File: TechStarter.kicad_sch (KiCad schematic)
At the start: 3 parts, among them U1 STM32F446RETx, U2 TMC2209-LA, U3 TMC2209-LA

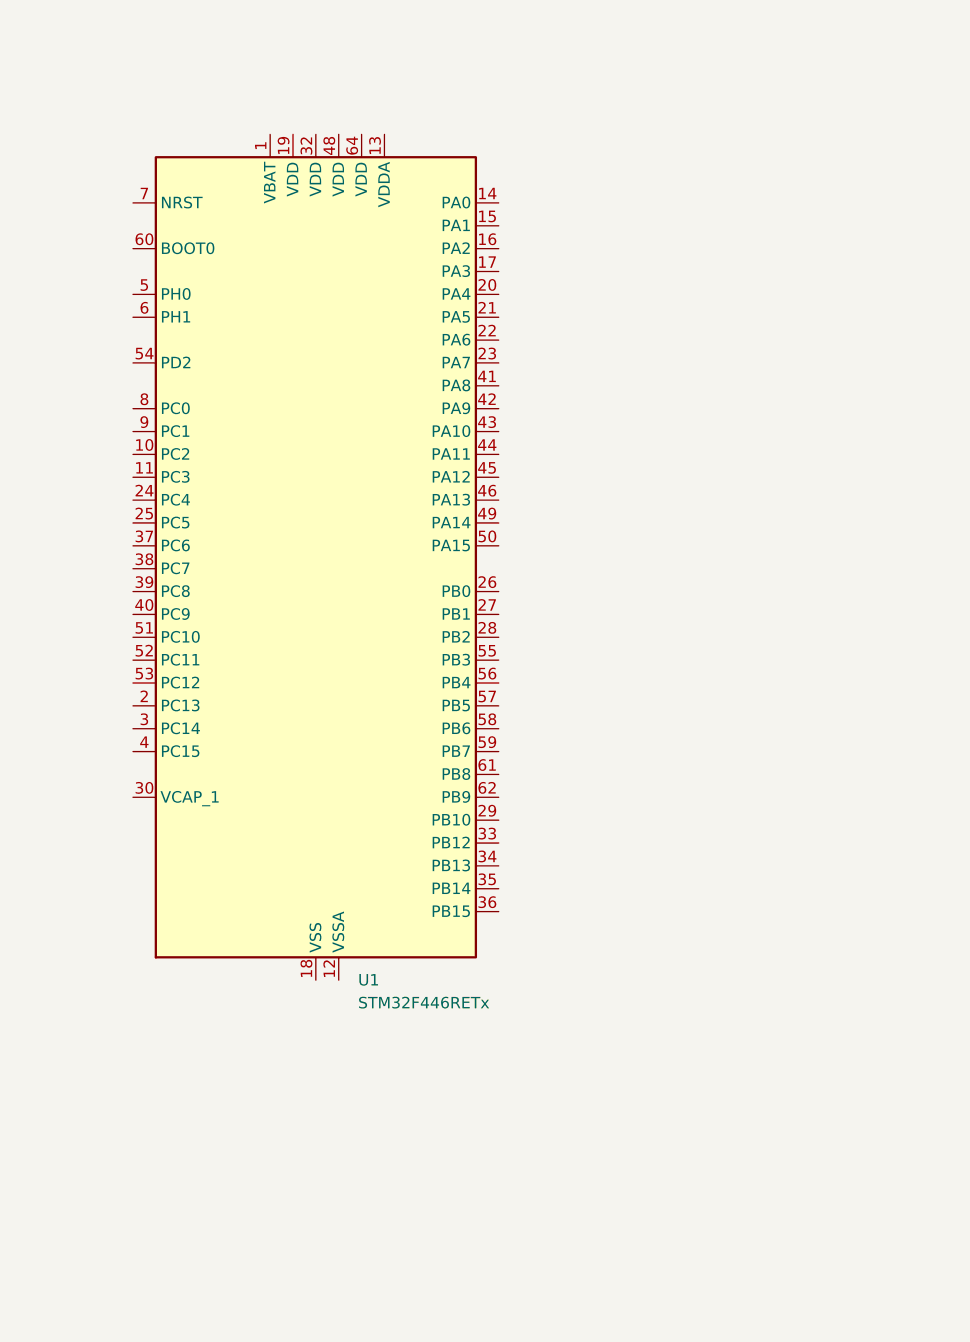
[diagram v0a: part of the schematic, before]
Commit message: added start of power brick
without values
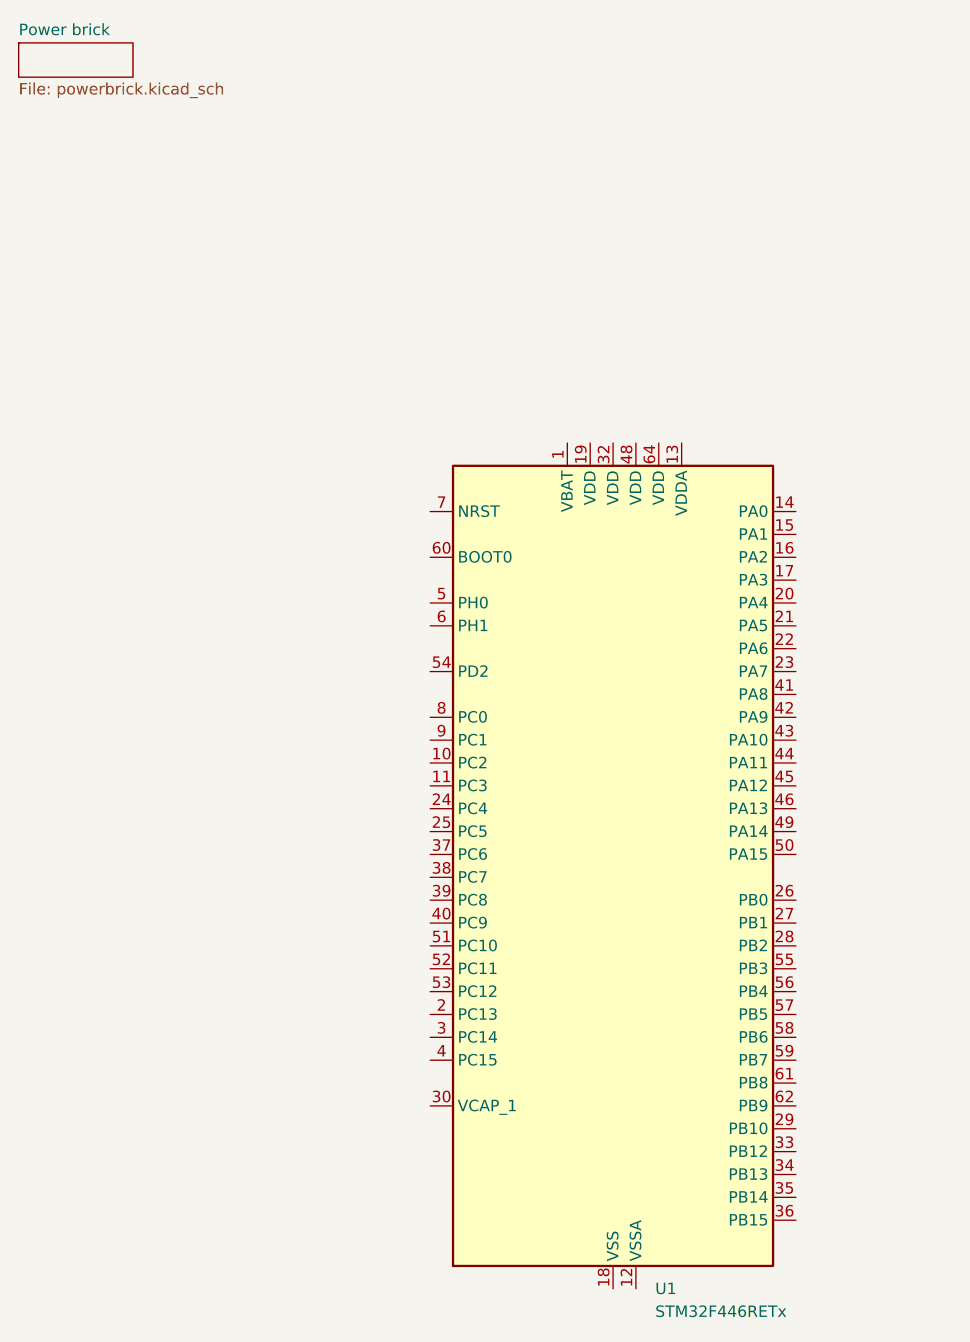
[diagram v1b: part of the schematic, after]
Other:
- added sheet Power brick (powerbrick.kicad_sch)
- moved on the sheet: U1
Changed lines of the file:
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@@
 	(symbol
 		(lib_id "MCU_ST_STM32F4:STM32F446RETx")
-		(at 54.61 80.01 0)
+		(at 87.63 114.3 0)
 		(unit 1)
 		(exclude_from_sim no)
@@
 		(fields_autoplaced yes)
 		(property "Reference" "U1"
-			(at 59.2933 125.73 0)
+			(at 92.3133 160.02 0)
 			(effects
 				(font
@@
 		)
 		(property "Value" "STM32F446RETx"
-			(at 59.2933 128.27 0)
+			(at 92.3133 162.56 0)
 			(effects
 				(font
@@
 		)
 		(property "Footprint" "Package_QFP:LQFP-64_10x10mm_P0.5mm"
-			(at 36.83 123.19 0)
+			(at 69.85 157.48 0)
 			(effects
 				(font
@@
 		)
 		(property "Datasheet" "https://www.st.com/resource/en/datasheet/stm32f446re.pdf"
-			(at 54.61 80.01 0)
+			(at 87.63 114.3 0)
 			(effects
 				(font
@@
 		)
 		(property "Description" "STMicroelectronics Arm Cortex-M4 MCU, 512KB flash, 128KB RAM, 180 MHz, 1.8-3.6V, 50 GPIO, LQFP64"
-			(at 54.61 80.01 0)
+			(at 87.63 114.3 0)
 			(effects
 				(font
@@
 				)
 			)
+		)
+	)
+	(sheet
+		(at 21.59 21.59)
+		(size 12.7 3.81)
+		(exclude_from_sim no)
+		(in_bom yes)
+		(on_board yes)
+		(dnp no)
+		(fields_autoplaced yes)
+		(stroke
+			(width 0.1524)
+			(type solid)
+		)
+		(fill
+			(color 0 0 0 0.0000)
+		)
+		(property "Sheetname" "Power brick"
+			(at 21.59 20.8784 0)
+			(effects
+				(font
+					(size 1.27 1.27)
+				)
+				(justify left bottom)
+			)
+		)
+		(property "Sheetfile" "powerbrick.kicad_sch"
+			(at 21.59 25.9846 0)
+			(effects
+				(font
+					(size 1.27 1.27)
+				)
+				(justify left top)
+			)
+		)
+		(instances
+			(project "TechStarter"
+				(path "/7ea2363f-6757-4fc6-83f2-16ce190d79d1"
+					(page "2")
+				)
+			)

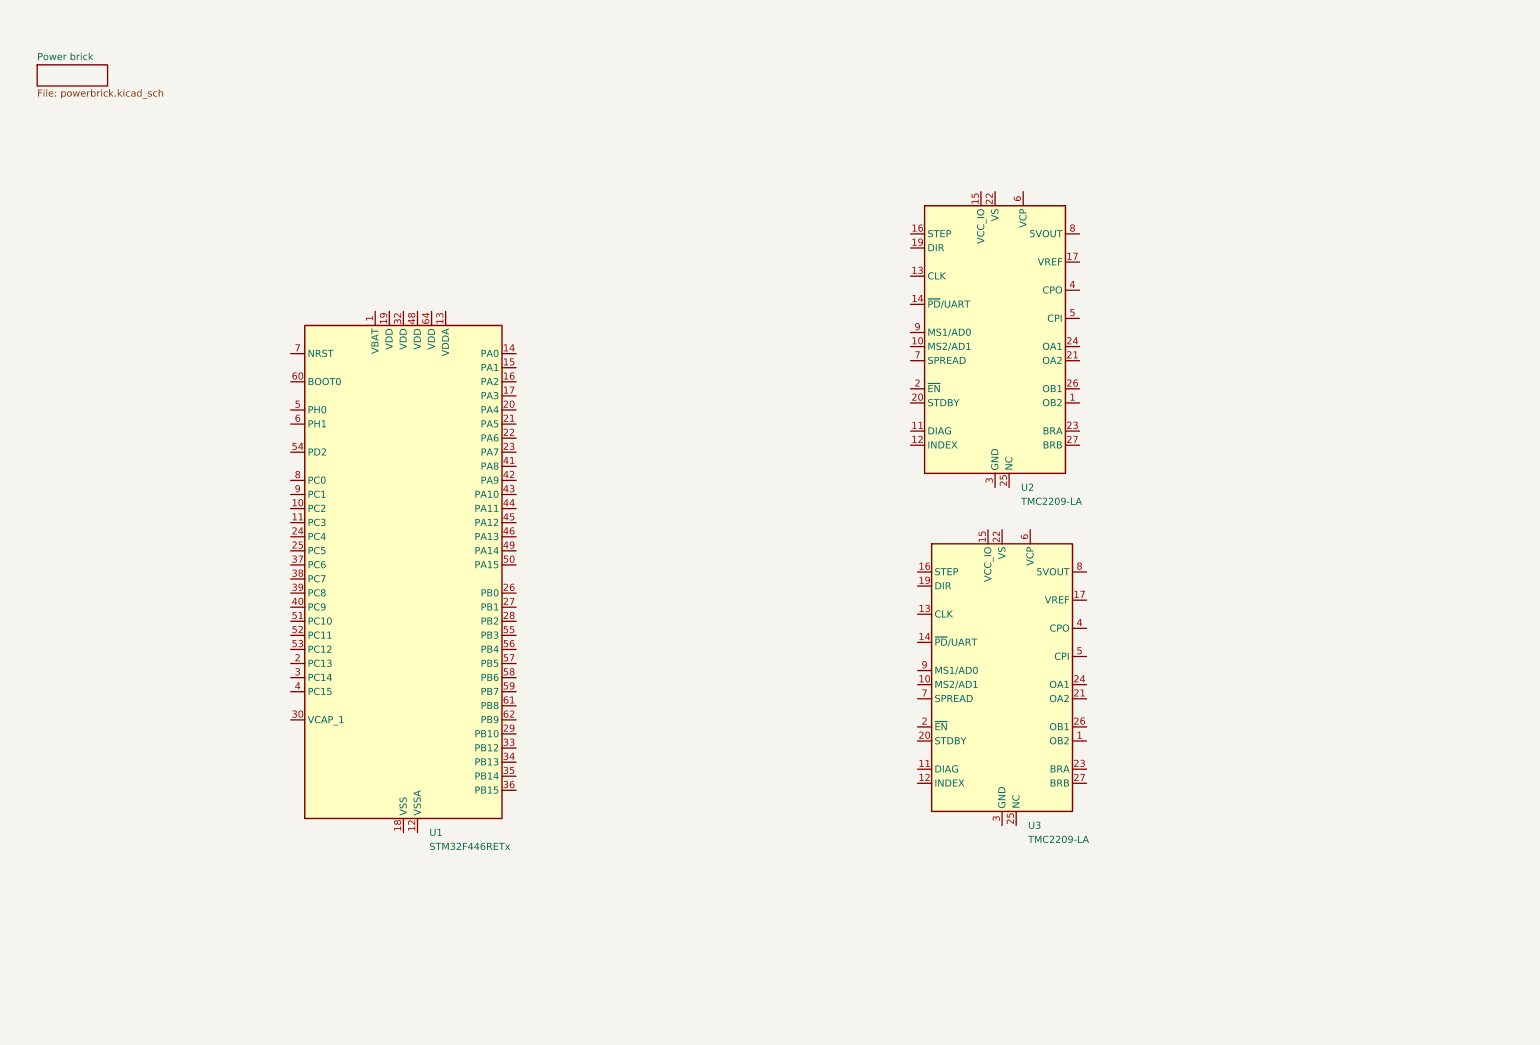
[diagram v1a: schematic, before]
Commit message: TMC2209
Zapojil jsem TMC2209 aby to fungírovalo  je tam zapojenej i enable pro nějakej pin na stm32 kdyby jsme je chtěli vypnout + uart může bejt zapojenej tak jak jsem ho zapojil protože pomocí MS1 a MS2 nastavuješ adresu a ten tvuj power brick je na vstupních 6 V ne na 24 V tak to vyřeš
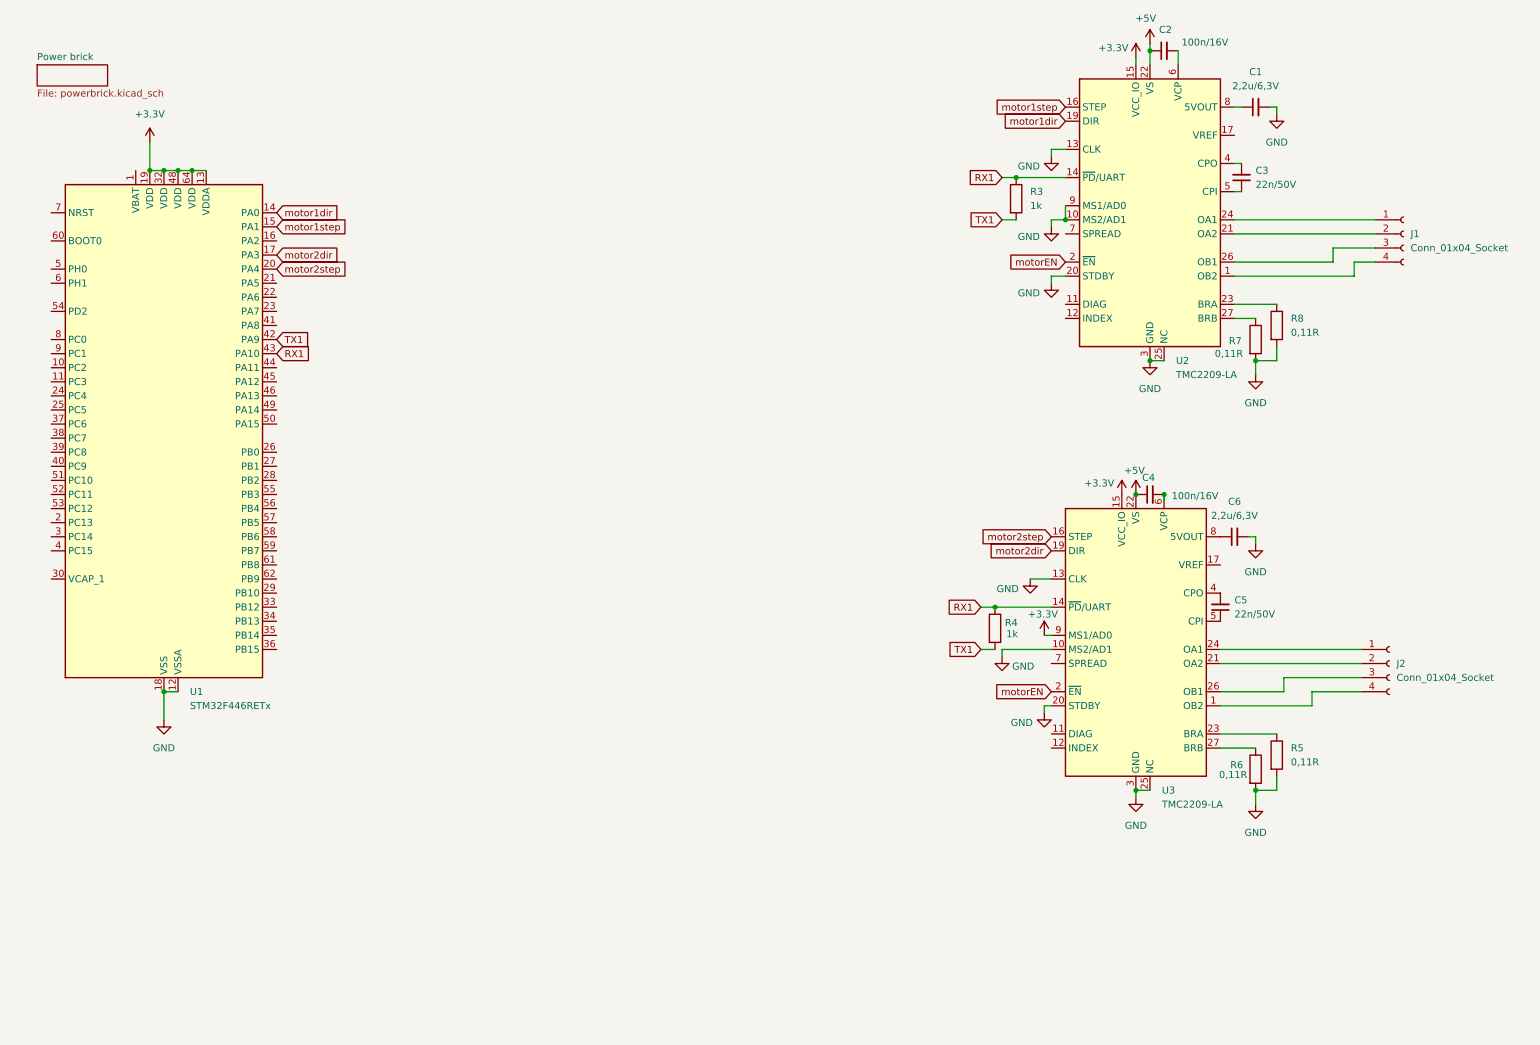
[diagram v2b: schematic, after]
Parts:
- added C1, C6: 2,2u/6,3V, symbol Device:C_Small
- added C2, C4: 100n/16V, symbol Device:C_Small
- added C3, C5: 22n/50V, symbol Device:C_Small
- added J1, J2: Conn_01x04_Socket, symbol Connector:Conn_01x04_Socket
- added R3, R4: 1k, symbol Device:R
- added R5, R6, R7, R8: 0,11R, symbol Device:R
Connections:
- net at U3.1 (OB2): now also J2.4 (Pin_4)
- net GND: now reaches U3.10 (MS2/AD1)
- net GND: now also U1.12 (VSSA), U1.18 (VSS), U1.31 (VSS), U1.47 (VSS), U1.63 (VSS), U2.10 (MS2/AD1), U2.13 (CLK), U2.18 (GND), U2.20 (STDBY), U2.25 (NC), U2.29 (GND), U2.3 (GND), U2.9 (MS1/AD0), U3.13 (CLK), U3.18 (GND), U3.20 (STDBY), U3.25 (NC), U3.29 (GND), U3.3 (GND), C1.2, C6.2, R5.2, R6.2, R7.2, R8.2
- net RX1: now reaches U3.14 (~{PD}/UART)
- net RX1: now also U1.43 (PA10), U2.14 (~{PD}/UART), R3.1, R4.1
- net +3.3V: now reaches U3.15 (VCC_IO)
- net +3.3V: now also U1.13 (VDDA), U1.19 (VDD), U1.32 (VDD), U1.48 (VDD), U1.64 (VDD), U2.15 (VCC_IO), U3.9 (MS1/AD0)
- net motor2step: now reaches U3.16 (STEP)
- net motor2step: now also U1.20 (PA4)
- net motor2dir: now reaches U3.19 (DIR)
- net motor2dir: now also U1.17 (PA3)
- net motorEN: now reaches U3.2 (~{EN})
- net motorEN: now also U2.2 (~{EN})
- net at U3.21 (OA2): now also J2.2 (Pin_2)
- net +5V: now reaches U3.22 (VS), U3.28 (VS)
- net +5V: now also U2.22 (VS), U2.28 (VS), C2.1, C4.1
- net at U3.23 (BRA): now also R5.1
- net at U3.24 (OA1): now also J2.1 (Pin_1)
- net at U3.26 (OB1): now also J2.3 (Pin_3)
- net at U3.27 (BRB): now also R6.1
- net at U3.4 (CPO): now also C5.2
- net at U3.5 (CPI): now also C5.1
- net at U3.6 (VCP): now also C4.2
- net at U3.8 (5VOUT): now also C6.1
- net at U2.1 (OB2): now also J1.4 (Pin_4)
- net motor1step: now reaches U2.16 (STEP)
- net motor1step: now also U1.15 (PA1)
- net motor1dir: now reaches U2.19 (DIR)
- net motor1dir: now also U1.14 (PA0)
- net at U2.21 (OA2): now also J1.2 (Pin_2)
- net at U2.23 (BRA): now also R8.1
- net at U2.24 (OA1): now also J1.1 (Pin_1)
- net at U2.26 (OB1): now also J1.3 (Pin_3)
- net at U2.27 (BRB): now also R7.1
- net at U2.4 (CPO): now also C3.2
- net at U2.5 (CPI): now also C3.1
- net at U2.6 (VCP): now also C2.2
- net at U2.8 (5VOUT): now also C1.1
- net TX1: now reaches U1.42 (PA9)
- net TX1: now also R3.2, R4.2
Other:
- moved on the sheet: U1, U2, U3
